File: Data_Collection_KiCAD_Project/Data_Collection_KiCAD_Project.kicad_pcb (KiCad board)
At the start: 2 copper layers, 68 parts, among them J1 USB_B_Micro, J2 Conn_Coaxial, J3 L717SDC37P1ACH4F, Q1 SI1040X-T1-GE3, U1 LM317T, U2 USBLC6-2SC6, U3 MCP9808_MSOP, U4 MAX-8Q, U5 STM32L552CC, U6 W25Q32JVSS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

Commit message: Changed MCU and started pcb
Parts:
- removed U5: STM32L552CC, Package_QFP:LQFP-48_7x7mm_P0.5mm
- added IC1: STM32L562VET6Q, STM32L562VET6Q:STM32L562VET6Q, F.Cu at (327.7, 43.2)
- added JP1: VDDA Bridge, Jumper:SolderJumper-2_P1.3mm_Open_Pad1.0x1.5mm, F.Cu at (372.1, 35.6)
- added JP2: VDD_SMPS, Jumper:SolderJumper-2_P1.3mm_Open_Pad1.0x1.5mm, F.Cu at (363.4, 42.2)
- added TP14: Debug Pad, TestPoint:TestPoint_Pad_D1.0mm, F.Cu at (362.8, 53.6)
- added TP15: Debug Pad, TestPoint:TestPoint_Pad_D1.0mm, F.Cu at (375.5, 41.9)
- added TP16: Debug Pad, TestPoint:TestPoint_Pad_D1.0mm, F.Cu at (366.3, 48.6)
- TP1, TP10, TP11, TP12, TP13, TP2, TP3, TP4, TP5, TP6, TP7, TP8, TP9: footprint TestPoint:TestPoint_Plated_Hole_D2.0mm -> TestPoint:TestPoint_Pad_D1.0mm
- moved C10 74.1 mm to (344.2, 54.1)
- moved C3 66.2 mm to (351.1, 75.5)
- moved U3 66.2 mm to (345.3, 76.5)
- moved R9 61.1 mm to (348.2, 54.1)
- moved C11 58.6 mm to (358.8, 49.2)
- moved C14 58.4 mm to (358.8, 51.7)
- moved C16 57.6 mm to (356.2, 54.2)
- moved C12 54.4 mm to (362.8, 45.2)
- moved C1 53.4 mm to (392.2, 52.1)
- moved R2 53.3 mm to (388.2, 52.2)
- moved R7 52.4 mm to (352.2, 54.1)
- moved R6 50.4 mm to (358.8, 46.7)
- moved D1 50.3 mm to (389.1, 49.5)
- moved U1 50.3 mm to (385.4, 43.3)
- moved C2 50.3 mm to (393.1, 49.5)
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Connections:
- J3 pad 22: /Main Bus/t_clk -> /SPI2_SCK

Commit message: PCB Progress
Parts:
- moved J3 229.6 mm to (92.9, 76.5), turned to 270 degrees
- moved IC1 65.4 mm to (392.8, 49.7)
- moved C23 48.8 mm to (386.9, 83.6)
- moved U9 48.8 mm to (390.7, 84.2)
- moved C10 46.0 mm to (389.7, 60.4)
- moved D3 46.0 mm to (404.5, 48.0)
- moved R10 46.0 mm to (413.1, 48.0)
- moved R9 46.0 mm to (393.7, 60.4)
- moved TP15 46.0 mm to (421.0, 48.3)
- moved TP16 46.0 mm to (411.8, 54.9)
- moved TP5 46.0 mm to (411.8, 51.9)
- moved TP7 46.0 mm to (421.0, 45.2)
- moved TP8 46.0 mm to (405.3, 60.8)
- moved C12 46.0 mm to (408.3, 51.6)
- moved C13 46.0 mm to (408.3, 54.1)
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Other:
- board outline added: 80 x 87.2 mm
- copper layers 2 -> 4
- net class Default: clearance 0.2 -> 0.15; trace_width 0.25 -> 0.2
- rule trace_clearance: 0.2 -> 0.15

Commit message: progress update
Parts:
- added TP17: Debug Pad, Connector_PinHeader_1.00mm:PinHeader_1x01_P1.00mm_Vertical, F.Cu at (85.8, 0.80)
- added TP18: Debug Pad, Connector_PinHeader_1.00mm:PinHeader_1x01_P1.00mm_Vertical, F.Cu at (85.8, 3.85)
- added TP19: Debug Pad, Connector_PinHeader_1.00mm:PinHeader_1x01_P1.00mm_Vertical, F.Cu at (89.1, 0.80)
- TP1, TP10, TP11, TP12, TP13, TP14, TP15, TP16, TP2, TP3, TP4, TP5, TP6, TP7, TP8, TP9: footprint TestPoint:TestPoint_Pad_D1.0mm -> Connector_PinHeader_1.00mm:PinHeader_1x01_P1.00mm_Vertical
- moved C15 315.5 mm to (103.2, 75.5), turned to 180 degrees
- moved C21 314.4 mm to (64.6, -21.7), turned to 90 degrees
- moved C19 307.2 mm to (70.1, -18.7), turned to 90 degrees
- moved C22 302.1 mm to (70.1, -14.7), turned to 90 degrees
- moved C20 300.6 mm to (72.7, -14.7), turned to 90 degrees
- moved C3 299.9 mm to (78.3, -16.6), turned to 90 degrees
- moved C16 299.2 mm to (103.2, 80.2), turned to 180 degrees
- moved Y1 298.4 mm to (109.8, 75.2), turned to 270 degrees
- moved Y2 298.1 mm to (64.7, -9.00), turned to 90 degrees
- moved C12 289.8 mm to (121.0, 89.2), turned to 180 degrees
- moved C13 287.3 mm to (121.2, 66.2)
- moved D3 286.4 mm to (124.6, -12.6)
- moved TP16 286.4 mm to (131.9, -5.71)
- moved TP5 286.4 mm to (131.9, -8.76)
- moved TP8 286.4 mm to (125.4, 0.22)
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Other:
- outline, holes or cut-outs redrawn

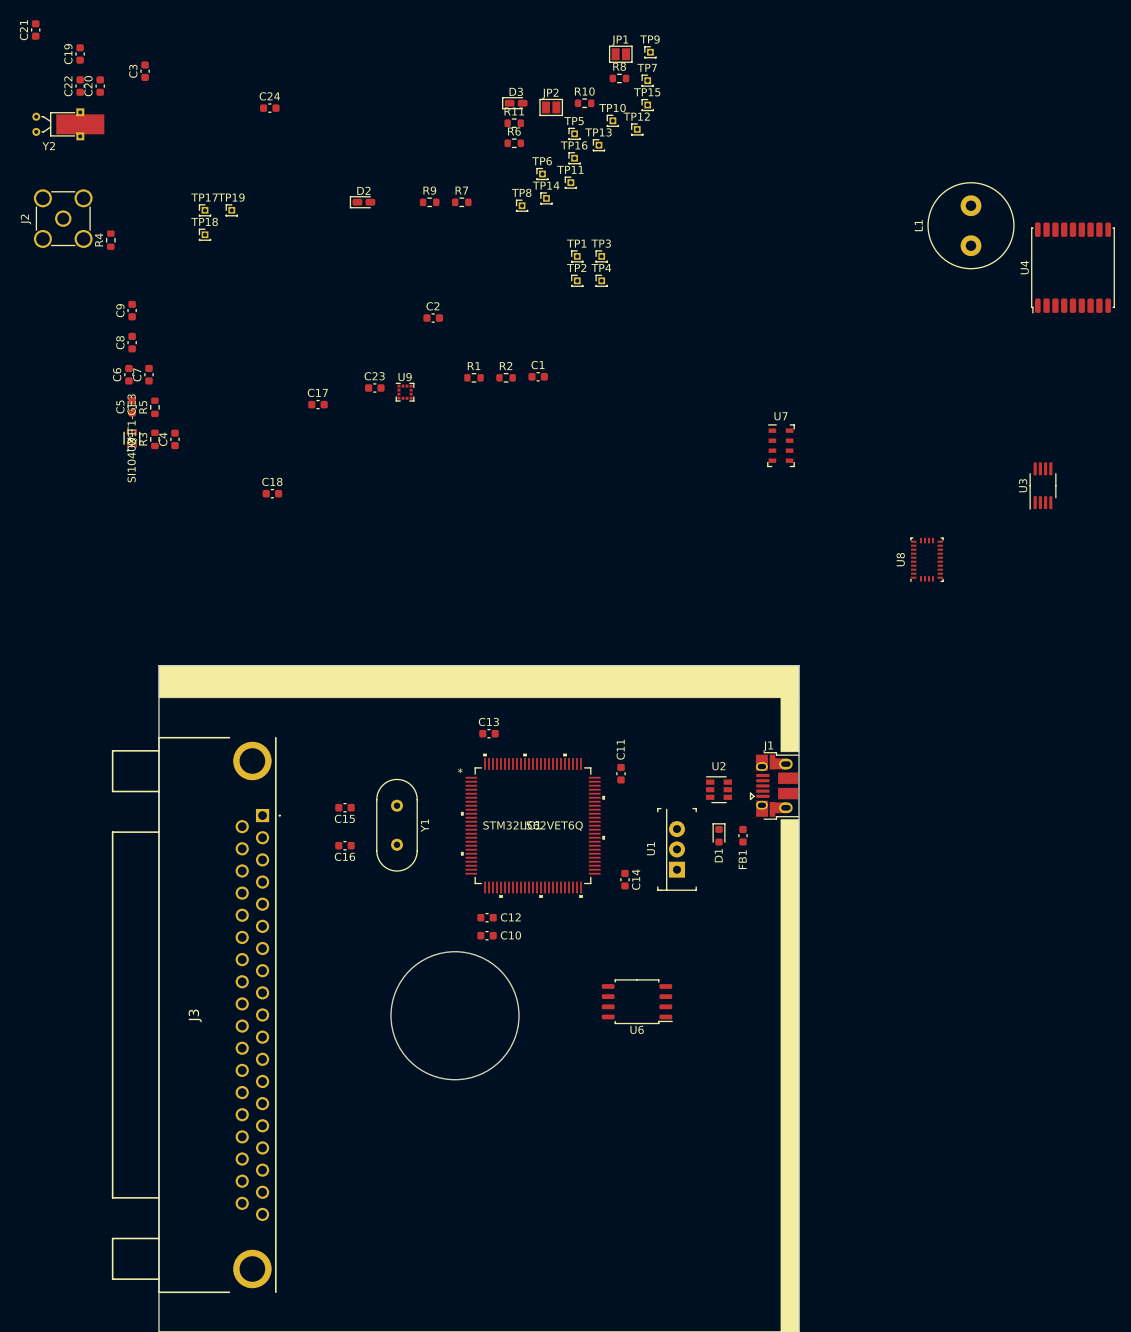
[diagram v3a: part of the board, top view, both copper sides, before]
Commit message: Finished laying out PCB Components
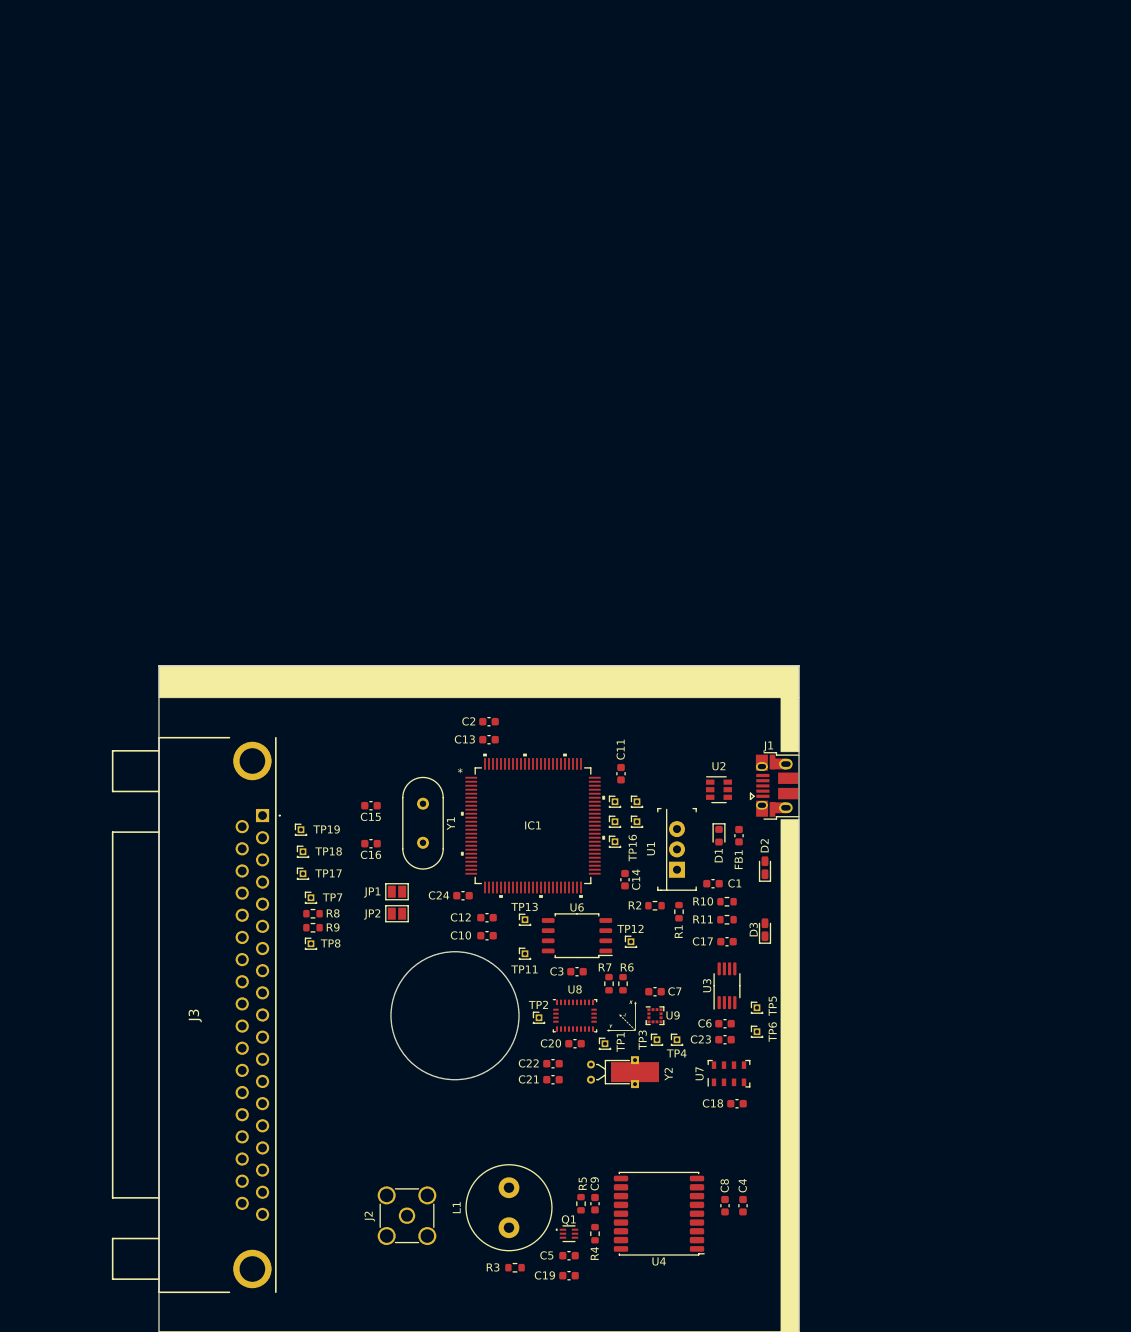
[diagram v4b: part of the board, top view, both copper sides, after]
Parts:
- added G***: LOGO, XYZ:XYZ_Plane, F.Cu at (137.8, 101.5)
- moved C19 164.5 mm to (131.2, 134.0), turned to 180 degrees
- moved C21 146.3 mm to (129.2, 109.5), turned to 0 degrees
- moved R4 138.2 mm to (134.5, 128.7), turned to 270 degrees
- moved Y2 137.3 mm to (134.0, 109.5)
- moved C22 135.7 mm to (129.2, 107.5), turned to 0 degrees
- moved L1 135.7 mm to (123.8, 128.0)
- moved C20 133.6 mm to (132.0, 105.0), turned to 180 degrees
- moved J2 131.8 mm to (111.0, 126.5)
- moved C8 130.9 mm to (150.8, 125.2), turned to 270 degrees
- moved U4 129.1 mm to (142.5, 126.2), turned to 180 degrees
- moved C9 125.7 mm to (134.5, 125.0)
- moved C3 124.8 mm to (132.2, 96.0), turned to 0 degrees
- moved C5 119.3 mm to (131.2, 131.5), turned to 0 degrees
- moved C4 119.2 mm to (153.0, 125.2), turned to 270 degrees
- moved Q1 113.5 mm to (131.2, 128.7), turned to 0 degrees
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
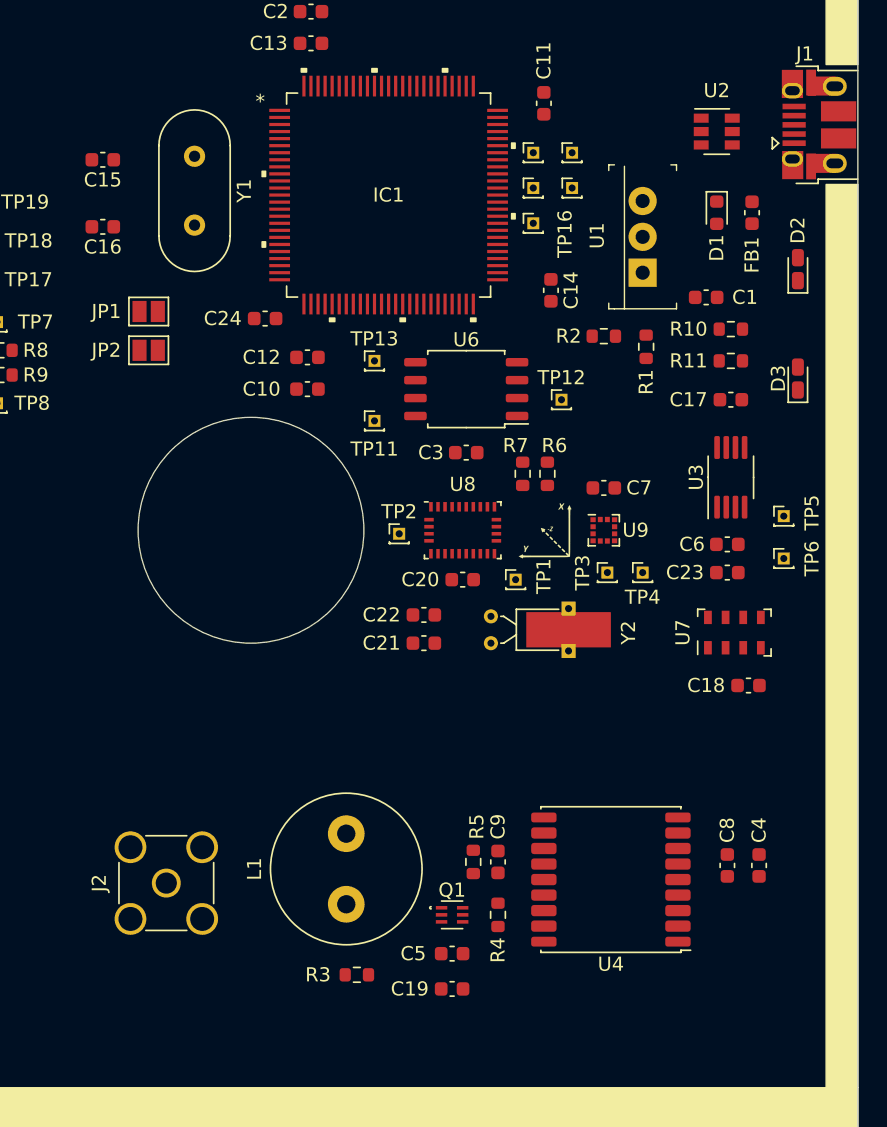
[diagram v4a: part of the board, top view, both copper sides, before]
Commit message: routed signal traces
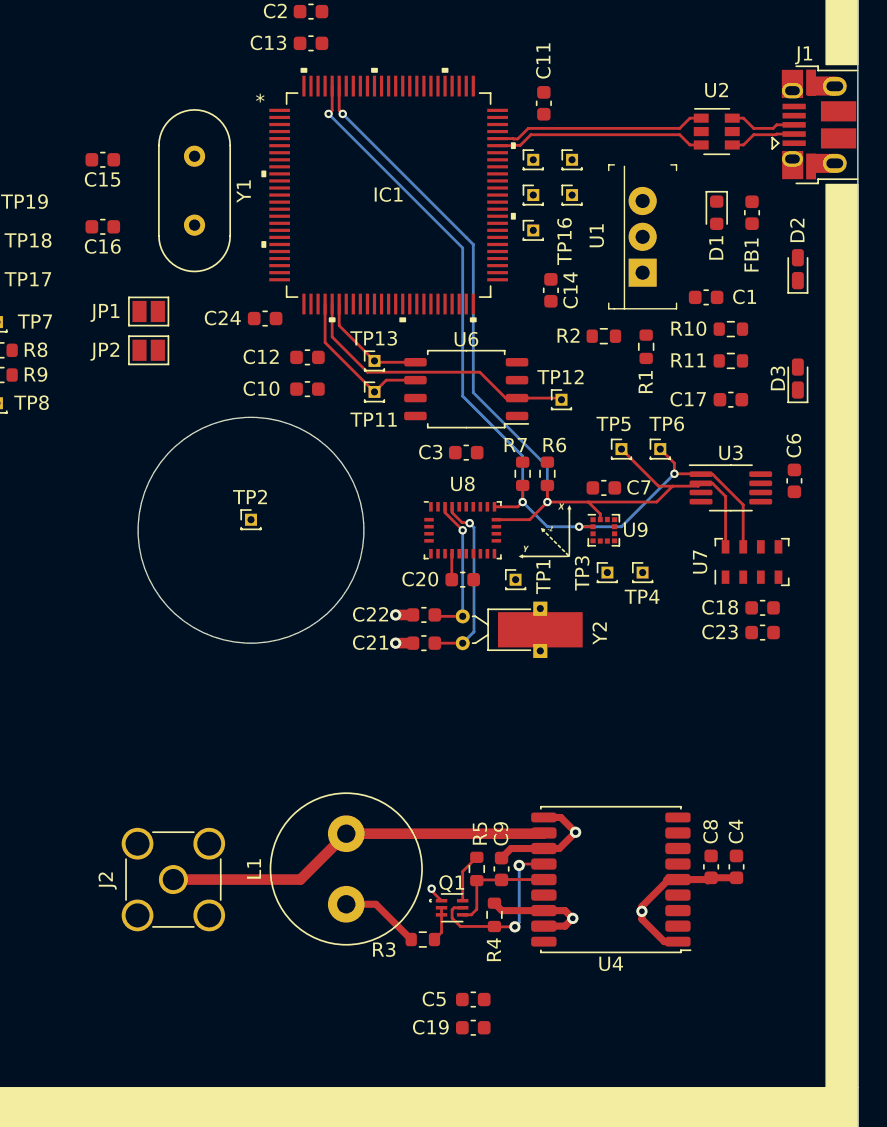
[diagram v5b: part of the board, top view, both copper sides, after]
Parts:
- moved TP5 12.4 mm to (143.2, 95.7)
- moved TP6 11.7 mm to (146.0, 95.7)
- moved TP2 10.5 mm to (117.0, 100.7)
- moved C6 6.54 mm to (155.5, 98.0), turned to 270 degrees
- moved C18 5.59 mm to (153.2, 107.0)
- moved R3 5.30 mm to (129.2, 130.5)
- moved U7 5.15 mm to (152.5, 103.7)
- moved C23 4.93 mm to (153.2, 108.7)
- moved C5 3.58 mm to (132.8, 134.7)
- moved C19 3.13 mm to (132.8, 136.7)
- moved TP11 2.05 mm to (125.8, 91.7)
- moved Y2 2.00 mm to (132.0, 109.5)
- moved C4 1.60 mm to (151.4, 125.3)
- moved C8 1.15 mm to (149.6, 125.3)
- moved U3 0.75 mm to (151.0, 98.5), turned to 0 degrees
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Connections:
- net /USB_DM renamed /USB_D-
- net /USB_DP renamed /USB_D+
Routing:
- net /I2C1_SCL: track 0.00 -> 64.3 mm, vias 0 -> 2
- net /I2C1_SDA: track 0.00 -> 63.5 mm, vias 0 -> 4
- net GND: track 0.00 -> 34.2 mm, vias 0 -> 6
- net /MAX-8Q/GPS_ANT_NET: track 0.00 -> 27.6 mm
- net /SPI1_MISO: track 0.00 -> 20.4 mm
- net /USB_D+: track 0.00 -> 15.0 mm
- net /USB_D-: track 0.00 -> 15.0 mm
- net Net-(C21-Pad2): track 0.00 -> 12.9 mm, vias 0 -> 1
- net /MAX-8Q/GPS_LNA_EN: track 0.00 -> 12.4 mm, vias 0 -> 2
- net /SPI1_SCK: track 0.00 -> 10.9 mm
- net Net-(C22-Pad2): track 0.00 -> 10.3 mm, vias 0 -> 1
- net /SPI1_MOSI: track 0.00 -> 8.00 mm
- net /MAX-8Q/GPS_VCC_RF: track 0.00 -> 7.98 mm
- net Net-(L1-Pad1): track 0.00 -> 6.56 mm
- net /USB Connector and ESD/USB_CONN_D+: track 0.00 -> 4.79 mm
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- added copper zone on In1.Cu, net GND

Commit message: routing update
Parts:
- moved TP2 10.3 mm to (127.2, 101.7)
- moved C19 9.89 mm to (142.2, 134.0), turned to 0 degrees
- moved C5 9.58 mm to (142.2, 136.0), turned to 180 degrees
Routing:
- net GND: track 34.2 -> 108.9 mm, vias 6 -> 20
- net /USART1_TX: track 0.00 -> 72.9 mm, vias 0 -> 1
- net /USART1_RX: track 0.00 -> 71.3 mm, vias 0 -> 1
- net +3V3: track 0.00 -> 66.8 mm, vias 0 -> 9
- net Net-(C15-Pad1): track 0.00 -> 12.8 mm
- net Net-(C16-Pad1): track 0.00 -> 12.7 mm
- net /EXT_SDA: track 0.00 -> 10.9 mm
- net /NRST: track 0.00 -> 9.55 mm
- net /SPI2_MOSI: track 0.00 -> 8.33 mm
- net /EXT_SCL: track 0.00 -> 8.21 mm
- net /SPI2_SCK: track 0.00 -> 7.74 mm
- net /SPI2_MISO: track 0.00 -> 5.48 mm
- net /BNO055/~BNO055_RESET: track 0.00 -> 4.58 mm
- net /KX134-1211/KX134_INT2: track 0.00 -> 3.65 mm
- net /KX134-1211/KX134_INT1: track 0.00 -> 2.44 mm
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- added copper zone on In2.Cu, net +3V3

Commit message: Routing Almost Finalized
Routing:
- net +3V3: track 66.8 -> 117.7 mm, vias 9 -> 13
- net GND: track 108.9 -> 157.6 mm, vias 20 -> 26
- net Net-(IC1-Pad2): track 0.00 -> 42.2 mm, vias 0 -> 2
- net Net-(IC1-Pad37): track 0.00 -> 27.4 mm, vias 0 -> 2
- net +5V: track 0.00 -> 18.5 mm
- net Net-(D2-Pad2): track 0.00 -> 10.0 mm
- net Net-(R1-Pad1): track 0.00 -> 6.73 mm
- net Net-(IC1-Pad63): track 0.00 -> 6.11 mm
- net Net-(FB1-Pad2): track 0.00 -> 5.83 mm
- net Net-(D3-Pad2): track 0.00 -> 4.11 mm
- net Net-(IC1-Pad62): track 0.00 -> 3.60 mm
- net Net-(IC1-Pad64): track 0.00 -> 2.74 mm
- net Net-(D1-Pad2): track 0.00 -> 2.51 mm
